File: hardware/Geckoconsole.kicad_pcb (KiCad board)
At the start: 2 copper layers, 83.1 x 43.2 mm, 55 parts, among them J1 Conn_01x06_Male, J11 Conn_01x06_Female, J31 Conn_01x07_Female, J50 USB-C, J51 Conn_01x06_Male, J70 I²C, J81 Conn_01x07, Q51 S8050, Q52 S8050, SW1 Reset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

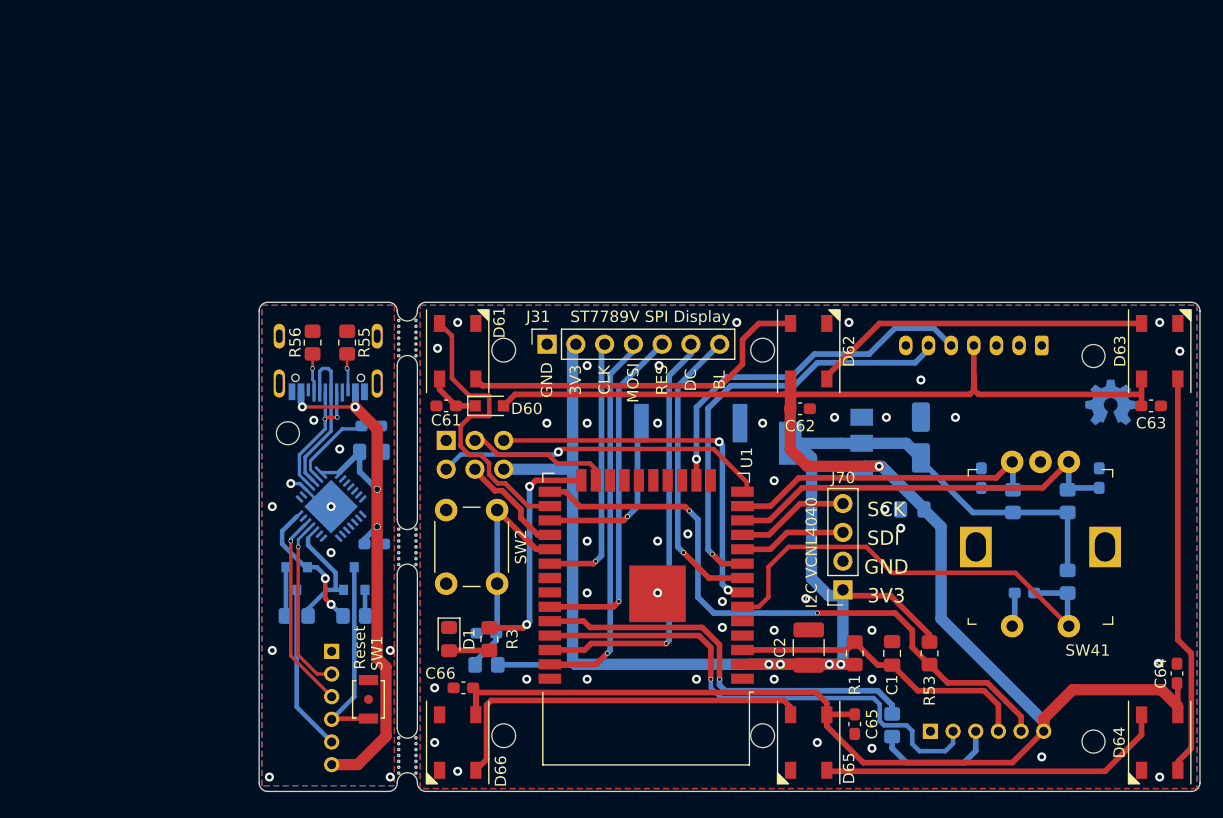
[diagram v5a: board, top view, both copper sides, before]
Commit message: PCB Console: Flip USB daugherboard, switch rotary encoder to SMD type
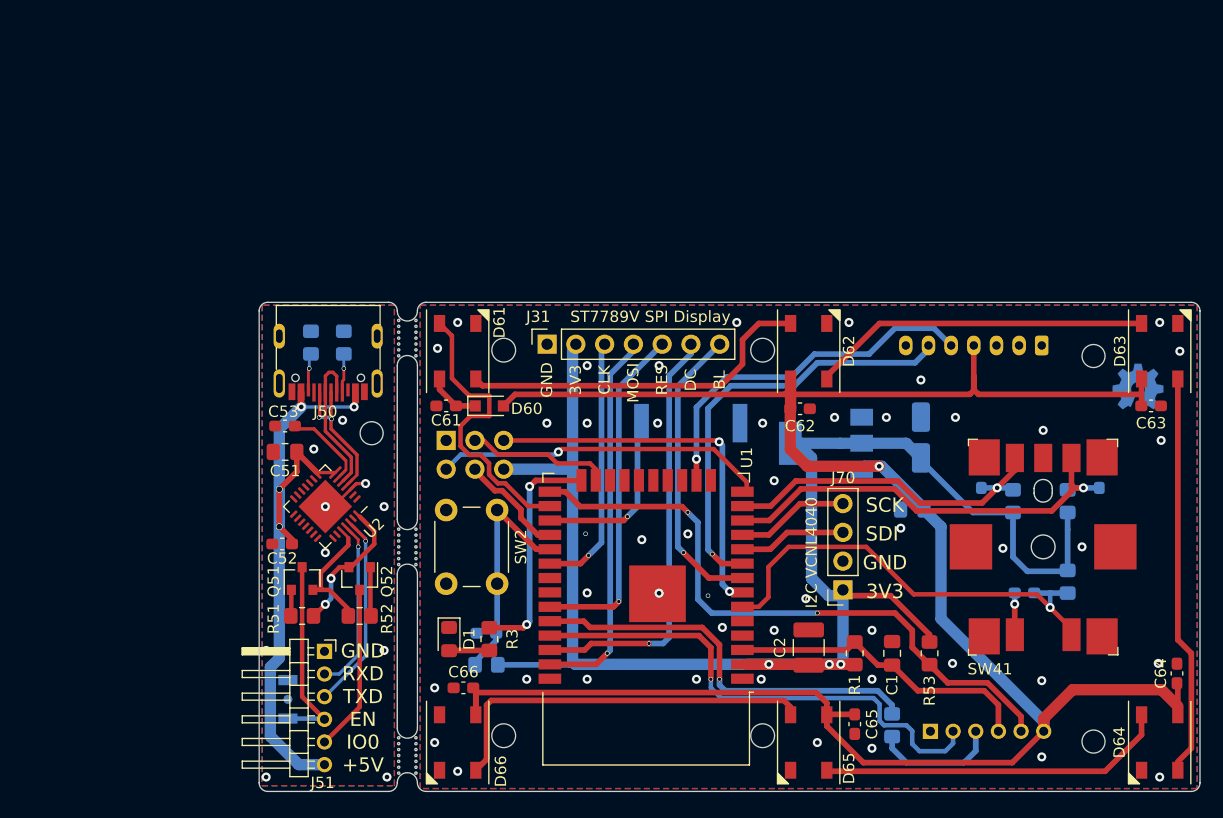
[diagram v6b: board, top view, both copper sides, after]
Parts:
- C51, C52, C53, J50, Q51, Q52, R51, R52, U2: moved to F.Cu
- J51: footprint Connector_PinHeader_2.00mm:PinHeader_1x06_P2.00mm_Horizontal -> Fraxinas:PinHeader_1x06_P2.00mm_Horizontal_Left; moved to F.Cu
- R55, R56, SW1: moved to B.Cu
- SW41: footprint Fraxinas:Rotary_Encoder_Switched_PEC11R -> Fraxinas:Rotary_Encoder_Switched_EC11J15
- moved C52 8.13 mm to (60.7, 81.3), turned to 180 degrees
- moved C51 7.62 mm to (61.0, 73.2), turned to 180 degrees
- moved C53 7.62 mm to (61.0, 70.9), turned to 0 degrees
- moved SW1 7.11 mm to (61.2, 95.0)
- moved J51 6.75 mm to (58.3, 90.8), turned to 0 degrees
- moved Q52 5.56 mm to (67.5, 84.3)
- moved R52 5.56 mm to (67.5, 87.6), turned to 180 degrees
- moved SW41 5.46 mm to (127.9, 81.5)
- moved Q51 4.60 mm to (62.5, 84.3)
- moved R51 4.60 mm to (62.5, 87.6), turned to 0 degrees
- moved R55 3.19 mm to (63.2, 63.5)
- moved LOGO1 2.79 mm to (136.3, 68.5)
- moved R56 2.76 mm to (66.1, 63.5)
- moved U2 0.51 mm to (64.5, 78.0), turned to -135 degrees
- moved G*** 0.19 mm to (94.3, 86.2)
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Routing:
- net +3V3: track 138.8 -> 143.3 mm, vias 4 -> 3
- net ENC_A: track 35.9 -> 37.9 mm, vias 0 -> 1
- net ENC_SW: track 41.0 -> 39.3 mm, vias 0 -> 1
- net /D-: track 14.0 -> 13.2 mm
- net SPI_CLK: track 23.2 -> 22.6 mm
- net ENC_B: track 30.4 -> 30.0 mm, vias 0 -> 1
- net Net-(C43-Pad2): track 3.03 -> 3.34 mm, vias 0 -> 1
- net GND: vias 42 -> 47
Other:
- outline, holes or cut-outs redrawn
- board text added: "USB Interface Board"

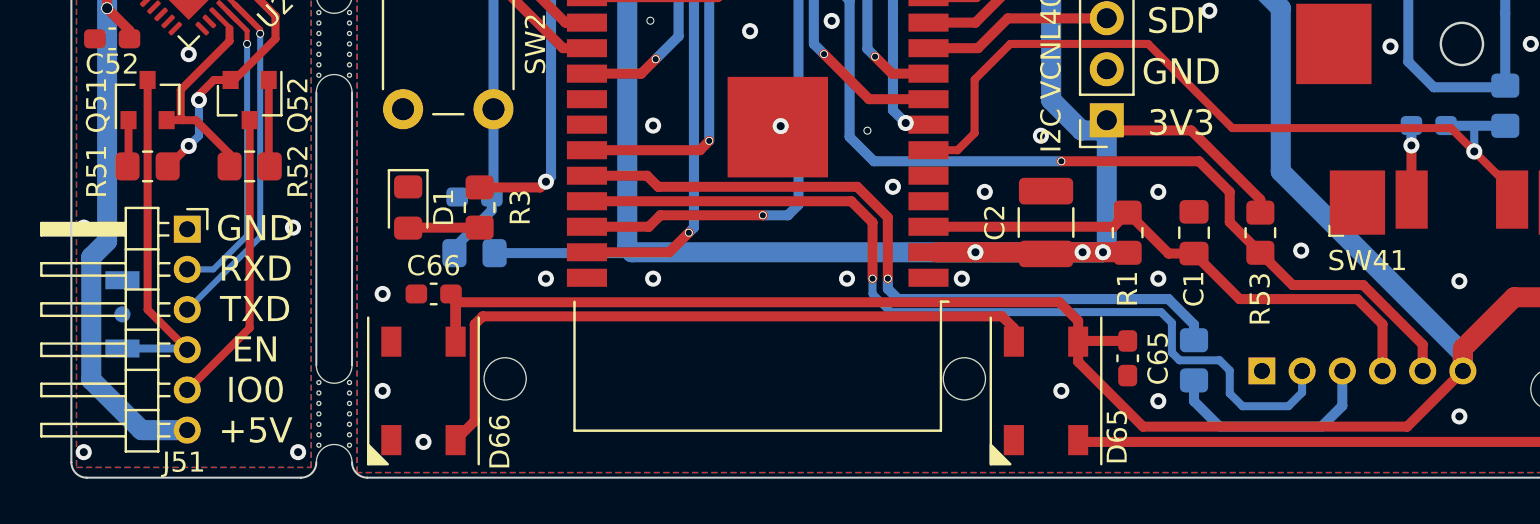
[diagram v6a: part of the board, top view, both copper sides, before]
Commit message: Hardware Console: Fix Encoder button (missing GND wire)
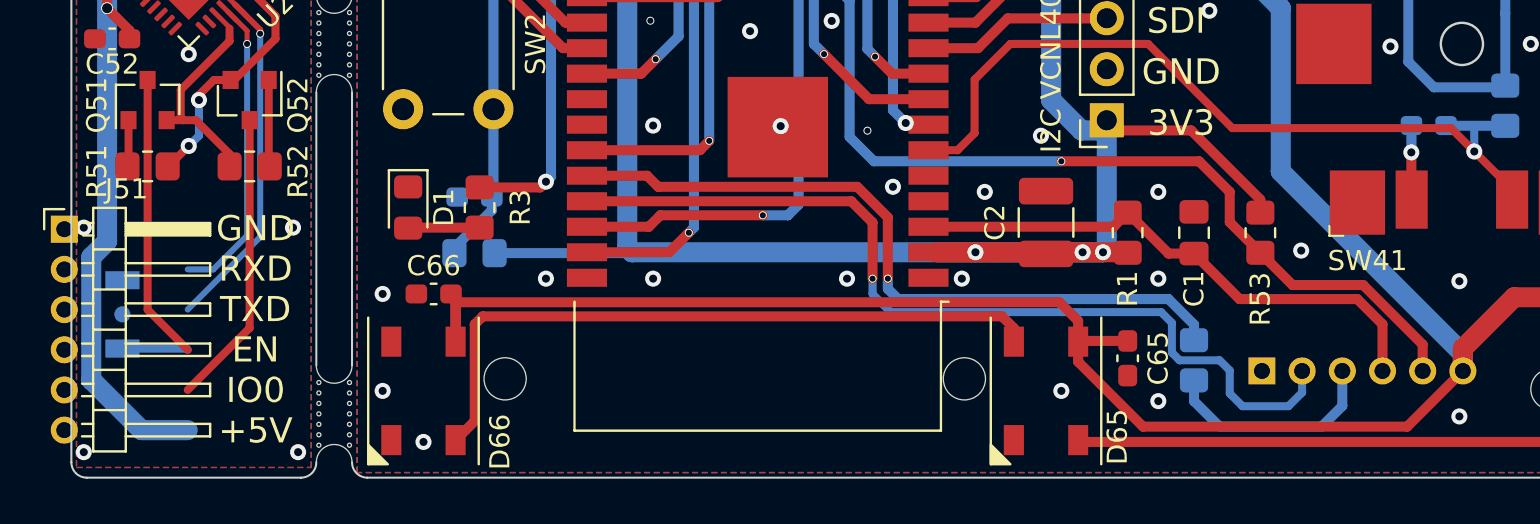
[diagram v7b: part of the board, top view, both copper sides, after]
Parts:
- J51: footprint Fraxinas:PinHeader_1x06_P2.00mm_Horizontal_Left -> Connector_PinHeader_2.00mm:PinHeader_1x06_P2.00mm_Horizontal
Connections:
- C43 pad 2: Net-(C43-Pad2) -> GND
- SW41 pad S2: Net-(C43-Pad2) -> GND
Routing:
- net GND: track 0.00 -> 3.35 mm, vias 47 -> 48
- net Net-(C43-Pad2): track 3.34 -> 0.00 mm, vias 1 -> 0

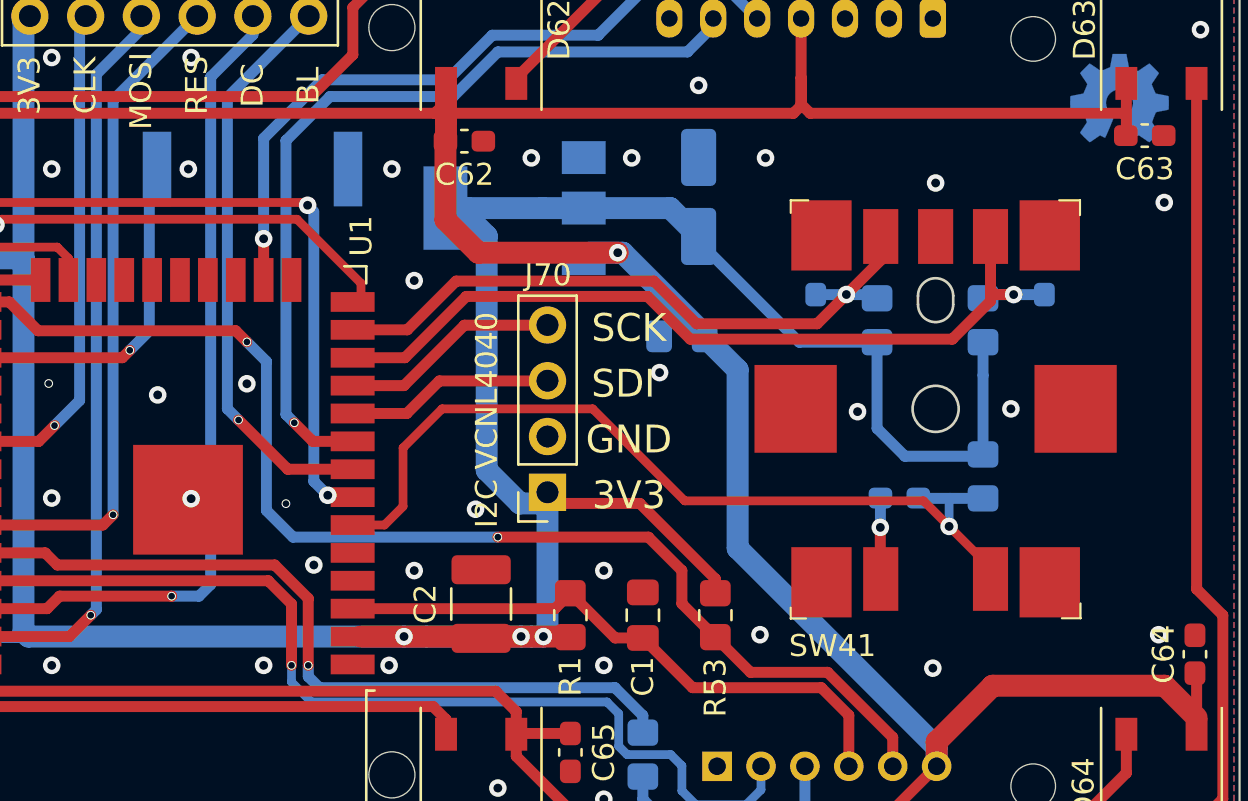
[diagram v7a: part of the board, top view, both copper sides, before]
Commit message: Hardware Console: Use new FUET Buzzer in schematic and PCB
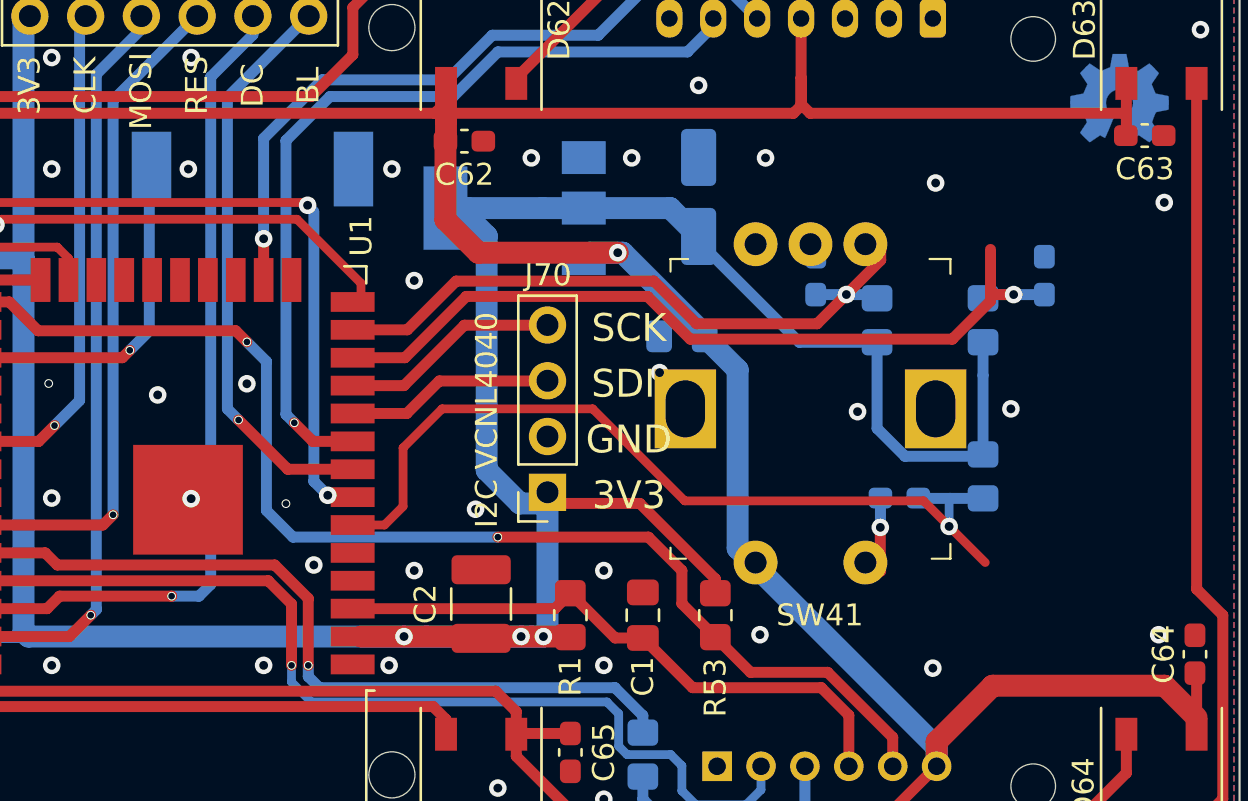
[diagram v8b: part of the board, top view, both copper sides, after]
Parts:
- BZ1: footprint Buzzer_Beeper:Buzzer_Murata_PKMCS0909E4000-R1 -> Fraxinas:Buzzer_FUET_9650B
- SW41: footprint Fraxinas:Rotary_Encoder_Switched_EC11J15 -> Fraxinas:Rotary_Encoder_Switched_PEC11R
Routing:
- net GND: track 3.35 -> 0.00 mm, vias 48 -> 47
- net ENC_SW: track 39.3 -> 42.7 mm, vias 1 -> 2
